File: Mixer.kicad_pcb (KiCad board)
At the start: 2 copper layers, 150 x 59 mm, 145 parts, among them J1 AudioJack3, J10 Conn_01x03, J11 Barrel_Jack_Switch, J2 AudioJack3, J3 USB_B_Micro, J4 Conn_01x03, J5 AudioJack3, J6 Conn_01x03, J7 AudioJack3, J8 Conn_01x03, J9 AudioJack3, SW1 SW_SPDT, SW2 SW_DPDT_x2, SW3 SW_DPDT_x2, U1 NJM4580CG, U10 NJM4580CG, U11 NJM4580CG, U12 SW_AKIDUKI, U2 NJM4580CG, U3 NJM4580CG, U4 MCW03, U5 MCW03, U6 NJM7809, U7 NJM7909, U8 NJM4580CG, U9 NJM4580CG

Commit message: 改版中
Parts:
- removed C48, C49: option_footprint, Capacitor_SMD:C_0603_1608Metric_Pad1.05x0.95mm_HandSolder
- removed G***: LOGO, toripoyo:tiemi
- removed J10, J6, J8: Conn_01x03, Connector_PinHeader_2.54mm:PinHeader_1x03_P2.54mm_Vertical
- removed RV2: RV10kA, toripoyo:RD925G-QA1
- added D14: 1N4148, Diode_SMD:D_SOD-123, F.Cu at (200.7, 110.5)
- added JP1: NoReg, Jumper:SolderJumper-2_P1.3mm_Open_TrianglePad1.0x1.5mm, F.Cu at (96.7, 128.3)
- added JP2: NoReg, Jumper:SolderJumper-2_P1.3mm_Open_TrianglePad1.0x1.5mm, F.Cu at (96.7, 131.8)
- added JP3: NoRect, Jumper:SolderJumper-2_P1.3mm_Open_TrianglePad1.0x1.5mm, F.Cu at (187.3, 146.0)
- added JP4: NoRect, Jumper:SolderJumper-2_P1.3mm_Open_TrianglePad1.0x1.5mm, F.Cu at (187.3, 151.0)
- added R23: 10k, Resistor_SMD:R_0603_1608Metric_Pad1.05x0.95mm_HandSolder, F.Cu at (162.3, 74.7)
- added R25: 10k, Resistor_SMD:R_0603_1608Metric_Pad1.05x0.95mm_HandSolder, F.Cu at (162.2, 77.6)
- added R26: 20k, Resistor_SMD:R_0603_1608Metric_Pad1.05x0.95mm_HandSolder, F.Cu at (197.6, 135.9)
- added R27: 10k, Resistor_SMD:R_0603_1608Metric_Pad1.05x0.95mm_HandSolder, F.Cu at (197.6, 138.4)
- added R28: 20k, Resistor_SMD:R_0603_1608Metric_Pad1.05x0.95mm_HandSolder, F.Cu at (202.0, 135.9)
- added R29: 10k, Resistor_SMD:R_0603_1608Metric_Pad1.05x0.95mm_HandSolder, F.Cu at (202.0, 138.4)
- added R30: 20k, Resistor_SMD:R_0603_1608Metric_Pad1.05x0.95mm_HandSolder, F.Cu at (206.3, 135.9)
- added R33: 20k, Resistor_SMD:R_0603_1608Metric_Pad1.05x0.95mm_HandSolder, F.Cu at (206.3, 138.4)
- added TP1: +9V, TestPoint:TestPoint_Pad_D1.5mm, F.Cu at (100.6, 128.3)
- added TP2: -9V, TestPoint:TestPoint_Pad_D1.5mm, F.Cu at (100.6, 131.8)
- added TP3: PH_L, TestPoint:TestPoint_Pad_D1.5mm, F.Cu at (193.0, 151.0)
- added TP4: PH_R, TestPoint:TestPoint_Pad_D1.5mm, F.Cu at (192.0, 147.0)
- C10, C11: value 4.7u -> 220u/6.3V; footprint Capacitor_THT:CP_Radial_D6.3mm_P2.50mm -> Capacitor_SMD:C_1210_3225Metric_Pad1.42x2.65mm_HandSolder; moved to B.Cu
- C12, C13, C18, C19: value 100u/16V -> 47u; footprint Capacitor_THT:CP_Radial_D5.0mm_P2.00mm -> Capacitor_SMD:C_1210_3225Metric_Pad1.42x2.65mm_HandSolder
- C14, C15: value 0.1u -> 47u; footprint Capacitor_SMD:C_0603_1608Metric_Pad1.05x0.95mm_HandSolder -> Capacitor_SMD:C_1210_3225Metric_Pad1.42x2.65mm_HandSolder; moved to F.Cu
- C16, C17: value 0.1u -> 47u; footprint Capacitor_SMD:C_0603_1608Metric_Pad1.05x0.95mm_HandSolder -> Capacitor_SMD:C_1210_3225Metric_Pad1.42x2.65mm_HandSolder
- C20: value 100u/6.3V -> 47u; footprint Capacitor_THT:CP_Radial_D5.0mm_P2.00mm -> Capacitor_SMD:C_1210_3225Metric_Pad1.42x2.65mm_HandSolder
- C21, C22, C23, C24: value 22u/16V -> 47u; footprint Capacitor_THT:CP_Radial_D5.0mm_P2.00mm -> Capacitor_SMD:C_1210_3225Metric_Pad1.42x2.65mm_HandSolder
- C35: value 0.47u -> 47u; footprint Capacitor_THT:CP_Radial_D5.0mm_P2.00mm -> Capacitor_SMD:C_1210_3225Metric_Pad1.42x2.65mm_HandSolder
- C36: value 22u/16V -> 220u/6.3V; footprint Capacitor_THT:CP_Radial_D5.0mm_P2.00mm -> Capacitor_SMD:C_1210_3225Metric_Pad1.42x2.65mm_HandSolder
- C39: value 22u/16V -> 22u/25V; footprint Capacitor_THT:CP_Radial_D5.0mm_P2.00mm -> Capacitor_SMD:C_0805_2012Metric_Pad1.15x1.40mm_HandSolder
- C40: value 0.47u -> 1u; footprint Capacitor_THT:C_Rect_L11.0mm_W4.2mm_P10.00mm_MKT -> Capacitor_SMD:C_0603_1608Metric_Pad1.05x0.95mm_HandSolder
- C41: value 0.47u -> 1u; footprint Capacitor_THT:C_Rect_L11.0mm_W4.2mm_P10.00mm_MKT -> Capacitor_SMD:C_0603_1608Metric_Pad1.05x0.95mm_HandSolder; moved to B.Cu
- C47: value 0.47u -> 22u/25V; footprint Capacitor_THT:CP_Radial_D5.0mm_P2.00mm -> Capacitor_SMD:C_0805_2012Metric_Pad1.15x1.40mm_HandSolder
- C50, C51: value option footprint -> 1u
- C53, C54, C55, C56: value 100u/16V -> 22u/25V; footprint Capacitor_THT:CP_Radial_D5.0mm_P2.00mm -> Capacitor_SMD:C_0805_2012Metric_Pad1.15x1.40mm_HandSolder
- D10, D12, D8, D9: value SS2040 -> 1N4148
- D11: value LED_RED -> LED_ORANGE
- D13: value LED_RED -> 1N4148; footprint LED_SMD:LED_0603_1608Metric_Pad1.05x0.95mm_HandSolder -> Diode_SMD:D_SOD-123
- J1, J2, J5, J7, J9: value AudioJack3 -> PJ-3420
- R13, R14: value 10k -> 33k
- R21, R24: value 470k -> 10k
- R31: value 4.7k -> 22k
- R32: value 4.7k -> 1.2k
- R35, R36: value 470 -> 1k
- R41, R42: value 100k -> 10k
- RV1, RV3, RV4, RV5: value RV10kA -> RK0972-A10K
- SW1: value SW_SPDT -> 2MS1-T1-B2-M7-S-E
- SW2, SW3: value SW_DPDT_x2 -> OS202011MA0QN1
- moved C35 98.9 mm to (100.3, 147.1), turned to 0 degrees
- moved C47 77.8 mm to (110.8, 146.4), turned to 0 degrees
- moved C41 35.9 mm to (171.2, 79.8), turned to 0 degrees
- moved C40 35.6 mm to (172.0, 76.2), turned to 90 degrees
- moved C16 14.0 mm to (103.5, 114.3)
- moved C17 14.0 mm to (86.4, 114.3)
- moved RV5 12.0 mm to (161.0, 114.0)
- moved C13 11.8 mm to (91.4, 89.3)
- moved C11 10.5 mm to (96.5, 81.9), turned to 180 degrees
- moved R35 6.84 mm to (196.8, 105.4)
- moved R36 6.38 mm to (200.7, 105.4)
- moved D13 6.25 mm to (196.8, 110.5)
- moved C14 6.21 mm to (106.0, 95.9)
- moved RV4 6.00 mm to (137.0, 114.0)
- moved C15 3.37 mm to (91.4, 95.9), turned to 90 degrees
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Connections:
- net BM64_MFB renamed BM62_MFB
- net BM64_SYS_PWR renamed BM62_SYS_PWR
- C20 pad 1: +5VD -> +9VA
- C20 pad 2: GND -> Net-(C20-Pad2)
- C21 pad 1: Net-(ANT1-Pad7) -> Net-(C20-Pad2)
- C21 pad 2: BT_in_R -> -9VA
- C22 pad 1: Net-(ANT1-Pad9) -> +9VA
- C22 pad 2: BT_in_L -> Net-(C20-Pad2)
- C23 pad 1: Net-(ANT1-Pad14) -> Net-(C20-Pad2)
- C23 pad 2: Net-(C23-Pad2) -> -9VA
- C24 pad 1: Net-(ANT1-Pad15) -> +9VA
- C24 pad 2: Net-(C24-Pad2) -> Net-(C20-Pad2)
- C35 pad 1: Net-(C35-Pad1) -> Net-(C20-Pad2)
- C35 pad 2: GND -> -9VA
- C36 pad 1: Net-(C36-Pad1) -> +5VD
- C37 pad 1: Net-(C36-Pad1) -> Net-(C37-Pad1)
- C39 pad 1: Net-(C38-Pad1) -> Net-(ANT1-Pad7)
- C39 pad 2: GND -> BT_in_R
- C45 pad 1: Net-(C45-Pad1) -> Net-(C40-Pad2)
- C46 pad 1: Net-(C46-Pad1) -> Net-(C41-Pad2)
- C47 pad 1: Net-(C47-Pad1) -> Net-(ANT1-Pad9)
- C47 pad 2: GND -> BT_in_L
- C50 pad 1: Net-(C40-Pad2) -> Net-(C50-Pad1)
- C50 pad 2: Net-(C40-Pad1) -> Net-(C50-Pad2)
- C51 pad 1: Net-(C41-Pad2) -> Net-(C51-Pad1)
- C51 pad 2: Net-(C41-Pad1) -> Net-(C51-Pad2)
- C53 pad 1: +9VA -> Net-(ANT1-Pad14)
- C53 pad 2: GND -> Net-(C53-Pad2)
- C54 pad 1: GND -> Net-(ANT1-Pad15)
- C54 pad 2: -9VA -> Net-(C54-Pad2)
- C55 pad 1: +9VA -> Net-(C37-Pad1)
- C56 pad 1: GND -> Net-(C38-Pad1)
- C56 pad 2: -9VA -> GND
- D10 pad 1: Net-(C47-Pad1) -> Net-(D10-Pad1)
- D12 pad 1: Net-(C35-Pad1) -> Net-(D12-Pad1)
- D13 pad 1: GND -> Net-(D11-Pad2)
- D2 pad 1: Net-(C24-Pad2) -> Net-(C54-Pad2)
- D5 pad 1: Net-(C23-Pad2) -> Net-(C53-Pad2)
- D8 pad 1: Net-(D10-Pad2) -> Net-(D8-Pad1)
- D8 pad 2: Net-(D8-Pad2) -> Net-(D10-Pad1)
- D9 pad 1: Net-(D12-Pad2) -> Net-(D9-Pad1)
- D9 pad 2: Net-(D9-Pad2) -> Net-(D12-Pad1)
- J9 pad R: Net-(C41-Pad1) -> Net-(C51-Pad2)
- J9 pad T: Net-(C40-Pad1) -> Net-(C50-Pad2)
- R15 pad 2: BT_Line_out_L -> mix_out_L
- R16 pad 2: BT_Line_out_R -> mix_out_R
- R19 pad 1: Net-(C23-Pad2) -> Net-(C53-Pad2)
- R19 pad 2: BT_Line_out_R -> mix_out_R
- R20 pad 1: Net-(C24-Pad2) -> Net-(C54-Pad2)
- R20 pad 2: BT_Line_out_L -> mix_out_L
- R21 pad 1: GND -> mix_out_L
- R21 pad 2: Net-(C47-Pad1) -> Net-(D8-Pad1)
- R24 pad 1: GND -> mix_out_R
- R24 pad 2: Net-(C35-Pad1) -> Net-(D9-Pad1)
- R36 pad 2: Net-(D11-Pad2) -> Net-(D14-Pad2)
- R37 pad 1: Net-(C36-Pad1) -> Net-(C37-Pad1)
- R38 pad 1: Net-(C36-Pad1) -> Net-(C37-Pad1)
- R38 pad 2: Net-(C40-Pad1) -> Net-(C50-Pad2)
- R39 pad 2: Net-(C41-Pad1) -> Net-(C51-Pad2)
- R41 pad 1: Net-(C40-Pad2) -> Net-(C50-Pad1)
- R42 pad 1: Net-(C41-Pad2) -> Net-(C51-Pad1)
- R46 pad 1: Net-(C45-Pad1) -> Net-(C40-Pad2)
- R47 pad 1: Net-(C46-Pad1) -> Net-(C41-Pad2)
- RV5 pad 3: Net-(C46-Pad1) -> Net-(C41-Pad1)
- RV5 pad 6: Net-(C45-Pad1) -> Net-(C40-Pad1)
- SW3 pad 1: Net-(C45-Pad1) -> Net-(C40-Pad2)
- SW3 pad 4: Net-(C46-Pad1) -> Net-(C41-Pad2)
- U10 pad 3: Net-(D8-Pad2) -> Net-(JP4-Pad2)
- U10 pad 5: Net-(D9-Pad2) -> Net-(JP3-Pad2)
- U11 pad 1: Net-(C45-Pad1) -> Net-(C40-Pad2)
- U11 pad 3: Net-(C40-Pad2) -> Net-(C50-Pad1)
- U11 pad 5: Net-(C41-Pad2) -> Net-(C51-Pad1)
- U11 pad 7: Net-(C46-Pad1) -> Net-(C41-Pad2)
- U8 pad 1: Net-(D12-Pad2) -> Net-(D12-Pad1)
- U8 pad 2: Net-(D9-Pad2) -> Net-(D9-Pad1)
- U8 pad 3: mix_out_R -> GND
- U8 pad 5: Net-(C35-Pad1) -> GND
- U8 pad 6: Net-(D9-Pad2) -> Net-(R28-Pad2)
- U8 pad 7: Net-(D9-Pad2) -> Net-(JP3-Pad2)
- U9 pad 1: Net-(D10-Pad2) -> Net-(D10-Pad1)
- U9 pad 2: Net-(D8-Pad2) -> Net-(D8-Pad1)
- U9 pad 3: mix_out_L -> GND
- U9 pad 5: Net-(C47-Pad1) -> GND
- U9 pad 6: Net-(D8-Pad2) -> Net-(R26-Pad2)
- U9 pad 7: Net-(D8-Pad2) -> Net-(JP4-Pad2)
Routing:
- net +9VA: track 258.6 -> 0.00 mm, vias 12 -> 0
- net -9VA: track 236.3 -> 0.00 mm, vias 9 -> 0
- net Net-(C46-Pad1): track 123.4 -> 0.00 mm, vias 2 -> 0
- net Net-(C45-Pad1): track 111.5 -> 0.00 mm, vias 2 -> 0
- net +5VD: track 108.0 -> 0.00 mm, vias 1 -> 0
- net BT_Line_out_L: track 94.2 -> 0.00 mm, vias 3 -> 0
- net BT_Line_out_R: track 91.3 -> 0.00 mm, vias 3 -> 0
- net mix_out_L: track 90.0 -> 0.00 mm
- net Net-(RV4-Pad3): track 88.9 -> 0.00 mm
- net Net-(RV4-Pad6): track 82.3 -> 0.00 mm
- net mix_out_R: track 84.8 -> 6.74 mm, vias 3 -> 0
- net BT_in_L: track 76.3 -> 0.00 mm
- net BT_in_R: track 74.9 -> 0.00 mm
- net Net-(J5-PadR): track 74.0 -> 0.00 mm, vias 1 -> 0
- net Net-(J5-PadT): track 70.1 -> 0.00 mm
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- added copper zone on B.Cu, net +9VA
- added copper zone on -V, net -9VA
- added copper zone on GND, net GND
- removed copper zone on B.Cu, net GND
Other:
- copper layers 2 -> 4
- board text removed: "Opt."
- board text removed: "To BT /Line Out"

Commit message: Rev.A 作成中
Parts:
- removed C23, C24, C35: 47u, Capacitor_SMD:C_1210_3225Metric_Pad1.42x2.65mm_HandSolder
- removed C3, C32, C37, C38, C52, C6, C9: 0.1u, Capacitor_SMD:C_0603_1608Metric_Pad1.05x0.95mm_HandSolder
- removed C36: 220u/6.3V, Capacitor_SMD:C_1210_3225Metric_Pad1.42x2.65mm_HandSolder
- removed C51: 1u, Capacitor_SMD:C_0603_1608Metric_Pad1.05x0.95mm_HandSolder
- removed C53, C54, C55, C56: 22u/25V, Capacitor_SMD:C_0805_2012Metric_Pad1.15x1.40mm_HandSolder
- removed D10, D13, D14, D8, D9: 1N4148, Diode_SMD:D_SOD-123
- removed D11: LED_ORANGE, LED_SMD:LED_0603_1608Metric_Pad1.05x0.95mm_HandSolder
- removed J11: Barrel_Jack_Switch, hastech:MJ-179P
- removed JP3, JP4: NoRect, Jumper:SolderJumper-2_P1.3mm_Open_TrianglePad1.0x1.5mm
- removed R43, R44: 1k, Resistor_SMD:R_0603_1608Metric_Pad1.05x0.95mm_HandSolder
- removed R45, R48: 10k, Resistor_SMD:R_0603_1608Metric_Pad1.05x0.95mm_HandSolder
- removed R46, R47: 100k, Resistor_SMD:R_0603_1608Metric_Pad1.05x0.95mm_HandSolder
- removed RV5: RK0972-A10K, toripoyo:RD925G-QA1
- removed TP1: +9V, TestPoint:TestPoint_Pad_D1.5mm
- removed TP2: -9V, TestPoint:TestPoint_Pad_D1.5mm
- removed TP3: PH_L, TestPoint:TestPoint_Pad_D1.5mm
- removed TP4: PH_R, TestPoint:TestPoint_Pad_D1.5mm
- removed U10: NJM4580CG, Package_SO:SOP-8_3.9x4.9mm_P1.27mm
- removed U12: SW_AKIDUKI, hastech:SW_AKZK
- added C48: 0.1u, Capacitor_SMD:C_0603_1608Metric_Pad1.05x0.95mm_HandSolder, F.Cu at (185.2, 80.5)
- added C49: 1u, Capacitor_SMD:C_0603_1608Metric_Pad1.05x0.95mm_HandSolder, F.Cu at (173.5, 79.0)
- added J10: Conn_01x03, Connector_PinSocket_2.54mm:PinSocket_1x03_P2.54mm_Vertical, F.Cu at (185.9, 92.5)
- added J6: PJ-3420, toripoyo:PJ-3420, F.Cu at (162.4, 57.4)
- added J8: PJ-3420, toripoyo:PJ-3420, F.Cu at (201.0, 57.3)
- added R34: 1k, Resistor_SMD:R_0603_1608Metric_Pad1.05x0.95mm_HandSolder, F.Cu at (191.3, 81.0)
- added RV2: RK0972-A10K, toripoyo:RD925G-QA1, F.Cu at (113.0, 114.0)
- C10: value 220u/6.3V -> 0.1u; footprint Capacitor_SMD:C_1210_3225Metric_Pad1.42x2.65mm_HandSolder -> Capacitor_SMD:C_0603_1608Metric_Pad1.05x0.95mm_HandSolder; moved to F.Cu
- C12: value 47u -> 220u/6.3V; moved to B.Cu
- C13, C14, C15, C16, C17, C18, C19, C20, JP1, JP2: moved to B.Cu
- C25: value 0.1u -> 47u; footprint Capacitor_SMD:C_0603_1608Metric_Pad1.05x0.95mm_HandSolder -> Capacitor_SMD:C_1210_3225Metric_Pad1.42x2.65mm_HandSolder; moved to F.Cu
- C26: value 0.1u -> 47u; footprint Capacitor_SMD:C_0603_1608Metric_Pad1.05x0.95mm_HandSolder -> Capacitor_SMD:C_1210_3225Metric_Pad1.42x2.65mm_HandSolder
- C27: value 0.1u -> 220u/6.3V; footprint Capacitor_SMD:C_0603_1608Metric_Pad1.05x0.95mm_HandSolder -> Capacitor_SMD:C_1210_3225Metric_Pad1.42x2.65mm_HandSolder; moved to B.Cu
- C28, C29, C30, C31, C42: value 0.1u -> 22u/25V; footprint Capacitor_SMD:C_0603_1608Metric_Pad1.05x0.95mm_HandSolder -> Capacitor_SMD:C_0805_2012Metric_Pad1.15x1.40mm_HandSolder
- C40: value 1u -> 0.1u
- C41: value 1u -> 0.1u; moved to F.Cu
- C43, C44: value 0.1u -> 1u
- C47: value 22u/25V -> 0.1u; footprint Capacitor_SMD:C_0805_2012Metric_Pad1.15x1.40mm_HandSolder -> Capacitor_SMD:C_0603_1608Metric_Pad1.05x0.95mm_HandSolder
- D12: value 1N4148 -> LED_ORANGE; footprint Diode_SMD:D_SOD-123 -> LED_SMD:LED_0603_1608Metric_Pad1.05x0.95mm_HandSolder
- J3: value USB_B_Micro -> Barrel_Jack_Switch; footprint toripoyo:USB_Micro_B_Female_10118193-0001LF -> hastech:MJ-179P
- J4: value Conn_01x03 -> USB_B_Micro; footprint Connector_PinHeader_2.54mm:PinHeader_1x03_P2.54mm_Vertical -> toripoyo:USB_Micro_B_Female_10118193-0001LF
- J5: value PJ-3420 -> Conn_01x03; footprint toripoyo:PJ-3420 -> Connector_PinHeader_2.54mm:PinHeader_1x03_P2.54mm_Vertical
- J9: value PJ-3420 -> Conn_01x03; footprint toripoyo:PJ-3420 -> Connector_PinSocket_2.54mm:PinSocket_1x03_P2.54mm_Vertical
- R1, R5: value 10 -> 47k
- R10, R9: value 47k -> 10k
- R11, R12, R24: value 10k -> 33k
- R13, R14: value 33k -> 600
- R15, R16: value 600 -> 10
- R18: moved to F.Cu
- R21: value 10k -> 2k; moved to B.Cu
- R22: value 2k -> 22k; moved to F.Cu
- R23, R42: value 10k -> 1.2k
- R25: value 10k -> 8.2k
- R26: value 20k -> 4.7k
- R27: value 10k -> 4.7
- R28: value 20k -> 2k?
- R29: value 10k -> 2k?
- R30: value 20k -> 4.7
- R31: value 22k -> 10k
- R32: value 1.2k -> 10k
- R33: value 20k -> 1k
- R35: value 1k -> 100k
- R36: value 1k -> 10k
- R37: value 4.7 -> 100k
- R38: value 2k? -> 10k
- R39: value 2k? -> 33k
- R40: value 4.7 -> 8.2k
- R41: value 10k -> 22k
- U8: value NJM4580CG -> SW_AKIDUKI; footprint Package_SO:SOP-8_3.9x4.9mm_P1.27mm -> hastech:SW_AKZK
- U9: value NJM4580CG -> LM339PWR; footprint Package_SO:SOP-8_3.9x4.9mm_P1.27mm -> Package_SO:TSSOP-14_4.4x5mm_P0.65mm
- moved C47 104.9 mm to (185.2, 72.4), turned to 180 degrees
- moved C26 101.8 mm to (85.7, 128.9), turned to 0 degrees
- moved R22 89.7 mm to (194.6, 96.8), turned to 90 degrees
- moved C28 78.8 mm to (114.0, 78.0), turned to 90 degrees
- moved U8 78.8 mm to (114.2, 63.0), turned to 180 degrees
- moved R16 78.0 mm to (213.1, 103.1), turned to 90 degrees
- moved R15 67.8 mm to (205.2, 102.9), turned to 90 degrees
- moved C21 65.9 mm to (79.5, 134.6)
- moved C27 65.9 mm to (126.0, 82.5), turned to 90 degrees
- moved R21 64.9 mm to (110.5, 65.3), turned to 0 degrees
- moved R33 64.4 mm to (179.1, 80.0), turned to 180 degrees
- moved C25 64.0 mm to (79.4, 128.9)
- moved R1 61.8 mm to (143.5, 97.3), turned to 270 degrees
- moved R29 59.9 mm to (209.3, 79.0)
- moved R28 59.2 mm to (218.2, 79.0)
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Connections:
- C10 pad 1: +5VD -> Net-(C10-Pad1)
- C12 pad 1: Net-(C12-Pad1) -> +5VD
- C13 pad 1: GND -> Net-(C13-Pad1)
- C13 pad 2: Net-(C13-Pad2) -> GND
- C14 pad 1: Net-(C12-Pad1) -> GND
- C14 pad 2: GND -> Net-(C14-Pad2)
- C15 pad 1: GND -> Net-(C13-Pad1)
- C15 pad 2: Net-(C13-Pad2) -> GND
- C16 pad 1: +9VA -> GND
- C16 pad 2: GND -> Net-(C14-Pad2)
- C17 pad 1: GND -> +9VA
- C17 pad 2: -9VA -> GND
- C18 pad 1: +9VA -> GND
- C18 pad 2: GND -> -9VA
- C19 pad 1: GND -> +9VA
- C19 pad 2: -9VA -> GND
- C20 pad 1: +9VA -> GND
- C20 pad 2: Net-(C20-Pad2) -> -9VA
- C21 pad 1: Net-(C20-Pad2) -> +9VA
- C21 pad 2: -9VA -> GND
- C22 pad 1: +9VA -> GND
- C22 pad 2: Net-(C20-Pad2) -> -9VA
- C25 pad 1: +5VD -> +9VA
- C26 pad 1: +9VA -> GND
- C26 pad 2: GND -> -9VA
- C27 pad 1: GND -> +5VD
- C27 pad 2: -9VA -> GND
- C28 pad 1: +9VA -> Net-(ANT1-Pad7)
- C28 pad 2: -9VA -> BT_in_R
- C29 pad 1: +9VA -> Net-(ANT1-Pad9)
- C29 pad 2: GND -> BT_in_L
- C30 pad 1: GND -> Net-(ANT1-Pad14)
- C30 pad 2: -9VA -> Net-(C30-Pad2)
- C31 pad 1: +9VA -> Net-(ANT1-Pad15)
- C31 pad 2: -9VA -> Net-(C31-Pad2)
- C33 pad 1: GND -> +9VA
- C33 pad 2: -9VA -> GND
- C34 pad 1: +9VA -> -9VA
- C34 pad 2: -9VA -> GND
- C39 pad 1: Net-(ANT1-Pad7) -> Net-(C39-Pad1)
- C39 pad 2: BT_in_R -> GND
- C40 pad 1: Net-(C40-Pad1) -> Net-(C39-Pad1)
- C40 pad 2: Net-(C40-Pad2) -> GND
- C41 pad 2: Net-(C41-Pad2) -> GND
- C42 pad 1: +9VA -> Net-(C41-Pad1)
- C43 pad 1: GND -> Net-(C43-Pad1)
- C43 pad 2: -9VA -> Net-(C43-Pad2)
- C44 pad 1: +9VA -> Net-(C44-Pad1)
- C44 pad 2: -9VA -> Net-(C44-Pad2)
- C45 pad 1: Net-(C40-Pad2) -> Net-(C45-Pad1)
- C46 pad 1: Net-(C41-Pad2) -> Net-(C46-Pad1)
- C47 pad 1: Net-(ANT1-Pad9) -> +9VA
- C47 pad 2: BT_in_L -> GND
- C50 pad 2: Net-(C50-Pad2) -> Net-(C46-Pad1)
- D2 pad 1: Net-(C54-Pad2) -> GND
- D3 pad 1: GND -> Net-(C30-Pad2)
- D4 pad 1: GND -> Net-(C31-Pad2)
- D5 pad 1: Net-(C53-Pad2) -> GND
- J3 pad 1: Net-(J11-Pad1) -> Net-(J3-Pad1)
- J3 pad 2: Net-(J3-Pad2) -> GND
- J3 pad 3: Net-(J3-Pad3) -> (no net)
- J4 pad 1: Net-(ANT1-Pad32) -> Net-(J3-Pad1)
- J4 pad 2: Net-(ANT1-Pad33) -> Net-(J4-Pad2)
- J4 pad 3: GND -> Net-(J4-Pad3)
- JP1 pad 1: Net-(C12-Pad1) -> Net-(C13-Pad1)
- JP2 pad 1: Net-(C13-Pad2) -> Net-(C14-Pad2)
- R1 pad 1: Net-(J2-PadT) -> Net-(R1-Pad1)
- R1 pad 2: Net-(R1-Pad2) -> in3_L
- R11 pad 1: Net-(R11-Pad1) -> mix_out_L
- R12 pad 1: Net-(R12-Pad1) -> mix_out_R
- R13 pad 1: mix_out_L -> Net-(J1-PadT)
- R13 pad 2: Net-(R11-Pad1) -> mix_out_L
- R14 pad 1: mix_out_R -> Net-(J1-PadR)
- R14 pad 2: Net-(R12-Pad1) -> mix_out_R
- R15 pad 1: Net-(J1-PadT) -> Net-(J2-PadT)
- R15 pad 2: mix_out_L -> Net-(R15-Pad2)
- R16 pad 1: Net-(J1-PadR) -> Net-(J2-PadR)
- R16 pad 2: mix_out_R -> Net-(R16-Pad2)
- R18 pad 1: Net-(J3-Pad2) -> Net-(J4-Pad2)
- R18 pad 2: Net-(J3-Pad3) -> Net-(J4-Pad3)
- R19 pad 1: Net-(C53-Pad2) -> Net-(C30-Pad2)
- R2 pad 1: Net-(R2-Pad1) -> Net-(R1-Pad1)
- R2 pad 2: in3_L -> in2_L
- R20 pad 1: Net-(C54-Pad2) -> Net-(C31-Pad2)
- R21 pad 1: mix_out_L -> GND
- R21 pad 2: Net-(D8-Pad1) -> BM62_MFB
- R22 pad 1: GND -> Net-(J9-Pad3)
- R22 pad 2: BM62_MFB -> +9VA
- R23 pad 1: Net-(D8-Pad1) -> GND
- R23 pad 2: Net-(D10-Pad2) -> Net-(J9-Pad3)
- R24 pad 1: mix_out_R -> Net-(J9-Pad1)
- R24 pad 2: Net-(D9-Pad1) -> +9VA
- R25 pad 1: Net-(D9-Pad1) -> GND
- R25 pad 2: Net-(D12-Pad2) -> Net-(J9-Pad1)
- R26 pad 1: mix_out_L -> +9VA
- R26 pad 2: Net-(R26-Pad2) -> Net-(D12-Pad2)
- R27 pad 1: Net-(D10-Pad2) -> Net-(C39-Pad1)
- R27 pad 2: Net-(R26-Pad2) -> +9VA
- R28 pad 1: mix_out_R -> Net-(C39-Pad1)
- R28 pad 2: Net-(R28-Pad2) -> Net-(C43-Pad2)
- R29 pad 1: Net-(D12-Pad2) -> Net-(C41-Pad1)
- R29 pad 2: Net-(R28-Pad2) -> Net-(C44-Pad2)
- R3 pad 1: Net-(R2-Pad1) -> Net-(R1-Pad1)
- R3 pad 2: in2_L -> in1_L
- R30 pad 1: Net-(R26-Pad2) -> Net-(C41-Pad1)
- R30 pad 2: Net-(JP4-Pad2) -> +9VA
- R31 pad 1: Net-(R31-Pad1) -> Net-(C43-Pad1)
- R31 pad 2: +9VA -> GND
- R32 pad 1: GND -> Net-(C44-Pad1)
- R32 pad 2: Net-(R31-Pad1) -> GND
- R33 pad 1: Net-(R28-Pad2) -> Net-(C45-Pad2)
- R33 pad 2: Net-(JP3-Pad2) -> GND
- R35 pad 1: Net-(R35-Pad1) -> Net-(C45-Pad1)
- R35 pad 2: Net-(D13-Pad2) -> Net-(C45-Pad2)
- R36 pad 2: Net-(D14-Pad2) -> Net-(C45-Pad2)
- R37 pad 1: Net-(C37-Pad1) -> Net-(C46-Pad1)
- R37 pad 2: +9VA -> Net-(C46-Pad2)
- R38 pad 1: Net-(C37-Pad1) -> Net-(R38-Pad1)
- R38 pad 2: Net-(C50-Pad2) -> Net-(C46-Pad2)
- R39 pad 1: Net-(C38-Pad1) -> Net-(J10-Pad1)
- R39 pad 2: Net-(C51-Pad2) -> GND
- R4 pad 1: Net-(R2-Pad1) -> Net-(R4-Pad1)
- R4 pad 2: in1_L -> in3_R
- R40 pad 1: Net-(C38-Pad1) -> -9VA
- R40 pad 2: +9VA -> Net-(J10-Pad1)
- R41 pad 1: Net-(C50-Pad1) -> Net-(J10-Pad3)
- R42 pad 1: Net-(C51-Pad1) -> -9VA
- R42 pad 2: GND -> Net-(J10-Pad3)
- R5 pad 1: Net-(J2-PadR) -> Net-(R4-Pad1)
- R5 pad 2: Net-(R5-Pad2) -> in2_R
- R6 pad 1: Net-(R10-Pad2) -> Net-(R4-Pad1)
- R6 pad 2: in3_R -> in1_R
- R7 pad 1: Net-(R10-Pad2) -> Net-(R7-Pad1)
- R7 pad 2: in2_R -> Net-(R1-Pad1)
- R8 pad 2: in1_R -> Net-(R4-Pad1)
- R9 pad 2: Net-(R2-Pad1) -> Net-(R7-Pad1)
- RV1 pad 3: mix_out_R -> mix_out_L
- RV1 pad 6: mix_out_L -> mix_out_R
- RV3 pad 2: in1_R -> in2_R
- RV3 pad 3: Net-(J5-PadR) -> Net-(RV3-Pad3)
- RV3 pad 5: in1_L -> in2_L
- RV3 pad 6: Net-(J5-PadT) -> Net-(RV3-Pad6)
- RV4 pad 2: in2_R -> in3_R
- RV4 pad 3: Net-(RV4-Pad3) -> Net-(C50-Pad1)
- RV4 pad 5: in2_L -> in3_L
- RV4 pad 6: Net-(RV4-Pad6) -> Net-(C49-Pad1)
- SW1 pad 1: Net-(J11-Pad1) -> Net-(J3-Pad1)
- SW2 pad 1: Net-(J7-PadT) -> Net-(J6-PadT)
- SW2 pad 2: Net-(RV4-Pad6) -> Net-(RV3-Pad6)
- SW2 pad 4: Net-(J7-PadR) -> Net-(J6-PadR)
- SW2 pad 5: Net-(RV4-Pad3) -> Net-(RV3-Pad3)
- SW3 pad 1: Net-(C40-Pad2) -> Net-(C45-Pad1)
- SW3 pad 2: Net-(R45-Pad1) -> Net-(R36-Pad1)
- SW3 pad 4: Net-(C41-Pad2) -> Net-(C46-Pad1)
- SW3 pad 5: Net-(R48-Pad1) -> Net-(R38-Pad1)
- U1 pad 1: Net-(R11-Pad2) -> Net-(R7-Pad1)
- U1 pad 2: Net-(R2-Pad1) -> Net-(R1-Pad1)
- U1 pad 6: Net-(R11-Pad1) -> Net-(R11-Pad2)
- U11 pad 1: Net-(C40-Pad2) -> Net-(C45-Pad1)
- U11 pad 3: Net-(C50-Pad1) -> Net-(C43-Pad1)
- U11 pad 5: Net-(C51-Pad1) -> Net-(C44-Pad1)
- U11 pad 7: Net-(C41-Pad2) -> Net-(C46-Pad1)
- U2 pad 1: Net-(R10-Pad1) -> Net-(R10-Pad2)
- U2 pad 2: Net-(R10-Pad2) -> Net-(R4-Pad1)
- U2 pad 6: Net-(R12-Pad1) -> Net-(R10-Pad1)
- U3 pad 1: Net-(R1-Pad2) -> Net-(R15-Pad2)
- U3 pad 2: Net-(R1-Pad2) -> Net-(R15-Pad2)
- U3 pad 3: Net-(RV1-Pad5) -> Net-(RV1-Pad2)
- U3 pad 5: Net-(RV1-Pad2) -> Net-(RV1-Pad5)
- U3 pad 6: Net-(R5-Pad2) -> Net-(R16-Pad2)
- U3 pad 7: Net-(R5-Pad2) -> Net-(R16-Pad2)
- U4 pad 6: Net-(C12-Pad1) -> Net-(C13-Pad1)
- U5 pad 7: Net-(C13-Pad2) -> Net-(C14-Pad2)
- U6 pad 1: Net-(C12-Pad1) -> Net-(C13-Pad1)
- U7 pad 2: Net-(C13-Pad2) -> Net-(C14-Pad2)
- U9 pad 1: Net-(D10-Pad1) -> Net-(D12-Pad1)
- U9 pad 2: Net-(D8-Pad1) -> Net-(D12-Pad1)
- U9 pad 3: GND -> +9VA
- U9 pad 4: -9VA -> vref_out_-
- U9 pad 5: GND -> mix_out_L
- U9 pad 6: Net-(R26-Pad2) -> mix_out_L
- U9 pad 7: Net-(JP4-Pad2) -> vref_out_+
- U9 pad 8: +9VA -> mix_out_R
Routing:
- net +5VD: track 0.00 -> 83.0 mm, vias 0 -> 1
- net Net-(J3-Pad1): track 0.00 -> 55.1 mm
- net Net-(J6-PadR): track 0.00 -> 25.7 mm
- net Net-(C13-Pad1): track 0.00 -> 23.5 mm
- net Net-(C14-Pad2): track 0.00 -> 21.0 mm
- net +9VA: track 0.00 -> 16.4 mm
- net -9VA: track 0.00 -> 15.4 mm
- net Net-(C10-Pad1): track 0.00 -> 14.2 mm
- net BM62_SYS_PWR: track 0.00 -> 13.6 mm
- net BM62_MFB: track 0.00 -> 8.86 mm
- net Net-(C39-Pad1): track 0.00 -> 8.75 mm
- net Net-(C41-Pad1): track 0.00 -> 8.75 mm
- net Net-(C45-Pad1): track 0.00 -> 6.96 mm
- net Net-(C46-Pad1): track 0.00 -> 6.85 mm
- net mix_out_R: track 6.74 -> 0.00 mm
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- added copper zone on B.Cu, net GND
- removed copper zone on B.Cu, net +9VA
- removed copper zone on -V, net -9VA
- removed copper zone on GND, net GND
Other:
- copper layers 4 -> 2
- board text added: "2020/8/24 poyo"
- board text removed: "2020/7/24 poyo"

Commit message: Rev.A 完成
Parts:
- removed C19, C20: 47u, Capacitor_SMD:C_1210_3225Metric_Pad1.42x2.65mm_HandSolder
- removed D5: VESD01-02V-G-08, Diode_SMD:D_SOD-523
- removed J10, J9: Conn_01x03, Connector_PinSocket_2.54mm:PinSocket_1x03_P2.54mm_Vertical
- removed U8: SW_AKIDUKI, hastech:SW_AKZK
- added C23: 0.1u, Capacitor_SMD:C_0603_1608Metric_Pad1.05x0.95mm_HandSolder, F.Cu at (153.0, 78.9)
- added C24: 0.1u, Capacitor_SMD:C_0603_1608Metric_Pad1.05x0.95mm_HandSolder, F.Cu at (150.5, 91.3)
- added C3: 0.1u, Capacitor_SMD:C_0603_1608Metric_Pad1.05x0.95mm_HandSolder, F.Cu at (165.7, 91.3)
- added C6: 0.1u, Capacitor_SMD:C_0603_1608Metric_Pad1.05x0.95mm_HandSolder, F.Cu at (153.0, 91.3)
- added C9: 0.1u, Capacitor_SMD:C_0603_1608Metric_Pad1.05x0.95mm_HandSolder, F.Cu at (165.7, 78.9)
- added R43: 4.7k, Resistor_SMD:R_0603_1608Metric_Pad1.05x0.95mm_HandSolder, F.Cu at (148.5, 101.9)
- added R44: 4.7k, Resistor_SMD:R_0603_1608Metric_Pad1.05x0.95mm_HandSolder, F.Cu at (146.4, 97.9)
- added R45: 4.7k, Resistor_SMD:R_0603_1608Metric_Pad1.05x0.95mm_HandSolder, F.Cu at (146.4, 101.9)
- added R46: 100, Resistor_SMD:R_0603_1608Metric_Pad1.05x0.95mm_HandSolder, F.Cu at (160.1, 78.9)
- added R47: 100, Resistor_SMD:R_0603_1608Metric_Pad1.05x0.95mm_HandSolder, F.Cu at (147.4, 78.9)
- added R48: 10k, Resistor_SMD:R_0603_1608Metric_Pad1.05x0.95mm_HandSolder, B.Cu at (210.7, 88.8)
- added R49: 10k, Resistor_SMD:R_0603_1608Metric_Pad1.05x0.95mm_HandSolder, B.Cu at (210.7, 91.7)
- added R50: 1k, Resistor_SMD:R_0603_1608Metric_Pad1.05x0.95mm_HandSolder, B.Cu at (215.2, 88.8)
- added R51: 1k, Resistor_SMD:R_0603_1608Metric_Pad1.05x0.95mm_HandSolder, B.Cu at (215.2, 91.7)
- added R52: 100, Resistor_SMD:R_0603_1608Metric_Pad1.05x0.95mm_HandSolder, F.Cu at (212.6, 88.8)
- added R53: 100, Resistor_SMD:R_0603_1608Metric_Pad1.05x0.95mm_HandSolder, F.Cu at (212.6, 90.8)
- added R54: 100, Resistor_SMD:R_0603_1608Metric_Pad1.05x0.95mm_HandSolder, F.Cu at (131.3, 99.8)
- added SW4: OS202011MA0QN1, digikey-download:OS202011MA0QN1, F.Cu at (215.4, 87.4)
- added SW5: OS202011MA0QN1, digikey-download:OS202011MA0QN1, F.Cu at (215.4, 74.6)
- added SW6: SW_Push, Button_Switch_THT:SW_PUSH_6mm, F.Cu at (115.8, 62.2)
- added U10: LM339PWR, Package_SO:TSSOP-14_4.4x5mm_P0.65mm, F.Cu at (151.0, 85.2)
- C13, C14, C15, C17, C18, C27: moved to F.Cu
- C25: value 47u -> 0.1u; footprint Capacitor_SMD:C_1210_3225Metric_Pad1.42x2.65mm_HandSolder -> Capacitor_SMD:C_0603_1608Metric_Pad1.05x0.95mm_HandSolder
- C26: value 47u -> 1u; footprint Capacitor_SMD:C_1210_3225Metric_Pad1.42x2.65mm_HandSolder -> Capacitor_SMD:C_0603_1608Metric_Pad1.05x0.95mm_HandSolder
- C30: value 22u/25V -> 1u; footprint Capacitor_SMD:C_0805_2012Metric_Pad1.15x1.40mm_HandSolder -> Capacitor_SMD:C_0603_1608Metric_Pad1.05x0.95mm_HandSolder
- C31: value 22u/25V -> 0.1u; footprint Capacitor_SMD:C_0805_2012Metric_Pad1.15x1.40mm_HandSolder -> Capacitor_SMD:C_0603_1608Metric_Pad1.05x0.95mm_HandSolder
- D12: value LED_ORANGE -> LED_RED
- D2, D4: value VESD01-02V-G-08 -> LED_GREEN; footprint Diode_SMD:D_SOD-523 -> LED_SMD:LED_0603_1608Metric_Pad1.05x0.95mm_HandSolder
- D3: value VESD01-02V-G-08 -> LED_RED; footprint Diode_SMD:D_SOD-523 -> LED_SMD:LED_0603_1608Metric_Pad1.05x0.95mm_HandSolder
- H1, H2, H3, H4: value MountingHole_Pad -> MountingHole; footprint MountingHole:MountingHole_3.2mm_M3_DIN965_Pad -> MountingHole:MountingHole_3.2mm_M3
- J3: value Barrel_Jack_Switch -> Conn_02x02_Counter_Clockwise; footprint hastech:MJ-179P -> Connector_PinHeader_2.54mm:PinHeader_2x02_P2.54mm_Vertical
- JP1: value NoReg -> UserShort; footprint Jumper:SolderJumper-2_P1.3mm_Open_TrianglePad1.0x1.5mm -> Jumper:SolderJumper-2_P1.3mm_Open_RoundedPad1.0x1.5mm
- JP2: value NoReg -> UserShort; footprint Jumper:SolderJumper-2_P1.3mm_Open_TrianglePad1.0x1.5mm -> Jumper:SolderJumper-2_P1.3mm_Open_RoundedPad1.0x1.5mm; moved to F.Cu
- R17: value 1k -> 4.7k
- R19: value 2k -> 33k
- R20: value 2k -> 1.2k
- R24: value 33k -> 1.2k
- R25: value 8.2k -> 33k
- R27, R30: value 4.7 -> 470
- R39: value 33k -> 100
- R40: value 8.2k -> 100
- moved H2 149.6 mm to (221.0, 64.0)
- moved H4 135.6 mm to (94.0, 115.0)
- moved C21 131.0 mm to (206.5, 102.5), turned to 270 degrees
- moved C22 121.7 mm to (202.4, 102.5), turned to 90 degrees
- moved C30 93.0 mm to (209.8, 89.7), turned to 90 degrees
- moved C25 87.0 mm to (150.5, 78.9), turned to 90 degrees
- moved C14 85.2 mm to (166.9, 101.0), turned to 180 degrees
- moved JP2 62.6 mm to (143.6, 83.3), turned to 0 degrees
- moved C13 61.6 mm to (166.9, 96.4)
- moved J3 50.8 mm to (127.8, 101.1), turned to 180 degrees
- moved R40 50.8 mm to (147.4, 91.3)
- moved C26 46.6 mm to (122.2, 99.8), turned to 90 degrees
- moved R24 45.9 mm to (155.8, 78.9)
- moved R25 45.9 mm to (155.8, 82.9)
- moved D2 40.2 mm to (156.8, 102.0)
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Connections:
- net Net-(J9-Pad1) renamed vref_out_-_-13dBv
- ANT1 pad 11: (no net) -> BT_Mic_Out_P
- ANT1 pad 12: (no net) -> BT_Mic_Out_N
- ANT1 pad 14: Net-(ANT1-Pad14) -> (no net)
- ANT1 pad 15: Net-(ANT1-Pad15) -> (no net)
- ANT1 pad 23: GND -> GNDD
- ANT1 pad 3: (no net) -> GNDD
- ANT1 pad 37: GND -> GNDD
- C10 pad 2: GND -> GNDD
- C11 pad 2: GND -> GNDD
- C12 pad 2: GND -> GNDD
- C13 pad 1: Net-(C13-Pad1) -> +9VA
- C13 pad 2: GND -> GND2
- C14 pad 1: GND -> GND2
- C14 pad 2: Net-(C14-Pad2) -> -9VA
- C15 pad 1: Net-(C13-Pad1) -> Net-(C15-Pad1)
- C16 pad 2: Net-(C14-Pad2) -> Net-(C16-Pad2)
- C25 pad 1: +9VA -> Net-(C25-Pad1)
- C25 pad 2: GND -> GND2
- C26 pad 2: -9VA -> BT_Mic_Out_N
- C27 pad 2: GND -> GNDD
- C30 pad 1: Net-(ANT1-Pad14) -> BT_Mic_Out_P
- C31 pad 1: Net-(ANT1-Pad15) -> GNDD
- C31 pad 2: Net-(C31-Pad2) -> GND
- C33 pad 1: +9VA -> Net-(C33-Pad1)
- C33 pad 2: GND -> GND2
- C34 pad 1: -9VA -> Net-(C34-Pad1)
- C34 pad 2: GND -> GND2
- D1 pad 1: GND -> -9VA
- D2 pad 1: GND -> Net-(D2-Pad1)
- D3 pad 1: Net-(C30-Pad2) -> Net-(D3-Pad1)
- D3 pad 2: Net-(D2-Pad2) -> Net-(D3-Pad2)
- D4 pad 1: Net-(C31-Pad2) -> Net-(D4-Pad1)
- H1 pad 1: GND -> (no net)
- H2 pad 1: GND -> (no net)
- H3 pad 1: GND -> (no net)
- H4 pad 1: GND -> (no net)
- J3 pad 1: Net-(J3-Pad1) -> GND
- J3 pad 3: (no net) -> GNDD
- J4 pad 1: Net-(J3-Pad1) -> Net-(J4-Pad1)
- J4 pad 5: GND -> GNDD
- J5 pad 3: GND -> GNDD
- JP1 pad 1: Net-(C13-Pad1) -> GND
- JP1 pad 2: +9VA -> GNDD
- JP2 pad 1: Net-(C14-Pad2) -> GND
- JP2 pad 2: -9VA -> GND2
- R17 pad 2: +5VD -> GND
- R19 pad 1: Net-(C30-Pad2) -> vref_out_+_-13dBv
- R19 pad 2: mix_out_R -> +9VA
- R20 pad 1: Net-(C31-Pad2) -> GND2
- R20 pad 2: mix_out_L -> vref_out_+_-13dBv
- R21 pad 1: GND -> GNDD
- R22 pad 1: Net-(J9-Pad3) -> vref_out_+_-10dBv
- R23 pad 1: GND -> GND2
- R23 pad 2: Net-(J9-Pad3) -> vref_out_+_-10dBv
- R24 pad 2: +9VA -> GND2
- R25 pad 1: GND -> -9VA
- R39 pad 1: Net-(J10-Pad1) -> Net-(C33-Pad1)
- R39 pad 2: GND -> +9VA
- R40 pad 1: -9VA -> Net-(C24-Pad1)
- R40 pad 2: Net-(J10-Pad1) -> +9VA
- R41 pad 1: Net-(J10-Pad3) -> -9VA
- R41 pad 2: GND -> vref_out_-_-10dBv
- R42 pad 1: -9VA -> vref_out_-_-10dBv
- R42 pad 2: Net-(J10-Pad3) -> GND2
- SW1 pad 1: Net-(J3-Pad1) -> Net-(J4-Pad1)
- U4 pad 1: GND -> GNDD
- U4 pad 6: Net-(C13-Pad1) -> Net-(C15-Pad1)
- U5 pad 1: GND -> GNDD
- U5 pad 7: Net-(C14-Pad2) -> Net-(C16-Pad2)
- U6 pad 1: Net-(C13-Pad1) -> Net-(C15-Pad1)
- U7 pad 2: Net-(C14-Pad2) -> Net-(C16-Pad2)
- U9 pad 10: vref_out_- -> vref_out_-_-10dBv
- U9 pad 12: -9VA -> Net-(C34-Pad1)
- U9 pad 13: Net-(D12-Pad1) -> Net-(D3-Pad1)
- U9 pad 14: Net-(D12-Pad1) -> Net-(D3-Pad1)
- U9 pad 3: +9VA -> Net-(C33-Pad1)
- U9 pad 4: vref_out_- -> vref_out_-_-10dBv
- U9 pad 7: vref_out_+ -> vref_out_+_-10dBv
- U9 pad 9: vref_out_+ -> vref_out_+_-10dBv
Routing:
- net +9VA: track 16.4 -> 240.8 mm, vias 0 -> 10
- net -9VA: track 15.4 -> 236.1 mm, vias 0 -> 11
- net mix_out_L: track 0.00 -> 169.1 mm, vias 0 -> 5
- net mix_out_R: track 0.00 -> 152.6 mm, vias 0 -> 7
- net BT_Mic_Out_P: track 0.00 -> 151.7 mm, vias 0 -> 2
- net in1_R: track 0.00 -> 79.6 mm
- net BT_in_R: track 0.00 -> 74.1 mm, vias 0 -> 1
- net BT_in_L: track 0.00 -> 73.7 mm, vias 0 -> 1
- net Net-(RV3-Pad3): track 0.00 -> 65.8 mm, vias 0 -> 2
- net Net-(RV3-Pad6): track 0.00 -> 60.2 mm, vias 0 -> 2
- net in1_L: track 0.00 -> 56.2 mm
- net Net-(J7-PadT): track 2.30 -> 58.0 mm, vias 0 -> 1
- net Net-(J3-Pad1): track 55.1 -> 0.00 mm
- net in2_R: track 0.00 -> 52.9 mm
- net Net-(J7-PadR): track 5.50 -> 57.3 mm, vias 0 -> 1
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- added copper zone on B.Cu, net GND2
- added copper zone on F.Cu, net GND2
- added copper zone on B.Cu, net GNDD
- added copper zone on F.Cu, net GNDD
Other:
- board size 150 x 59 mm -> 135 x 59 mm
- net class Default: via_dia 0.8 -> 1; via_drill 0.4 -> 0.6
- rule trace_min: 0.2 -> 0.254
- board text added: "-10dBv (Peak)"
- board text added: "-13dBv"
- board text added: "-Isolate |Common"
- board text added: "2020/11/24 Rev.A poyo"
- board text added: "BT Send Mix/Mic"
- board text added: "Bluetooth / Line 2"
- board text added: "GND Rx Tx"
- board text added: "L"
- board text added: "Line 1"
- board text added: "Line Mix Level"
- board text added: "Mic Gain 40dB/20dB"
- board text added: "Mic Mute UnMute/Mute"
- board text added: "Mic in (ECM)"
- board text added: "Monitor Out"
- board text added: "R"
- board text removed: "2020/8/24 poyo"
- board text removed: "40dB/20dB"
- board text removed: "DC5V only"
- board text removed: "Line in 2 / BT"
- board text removed: "Peak"

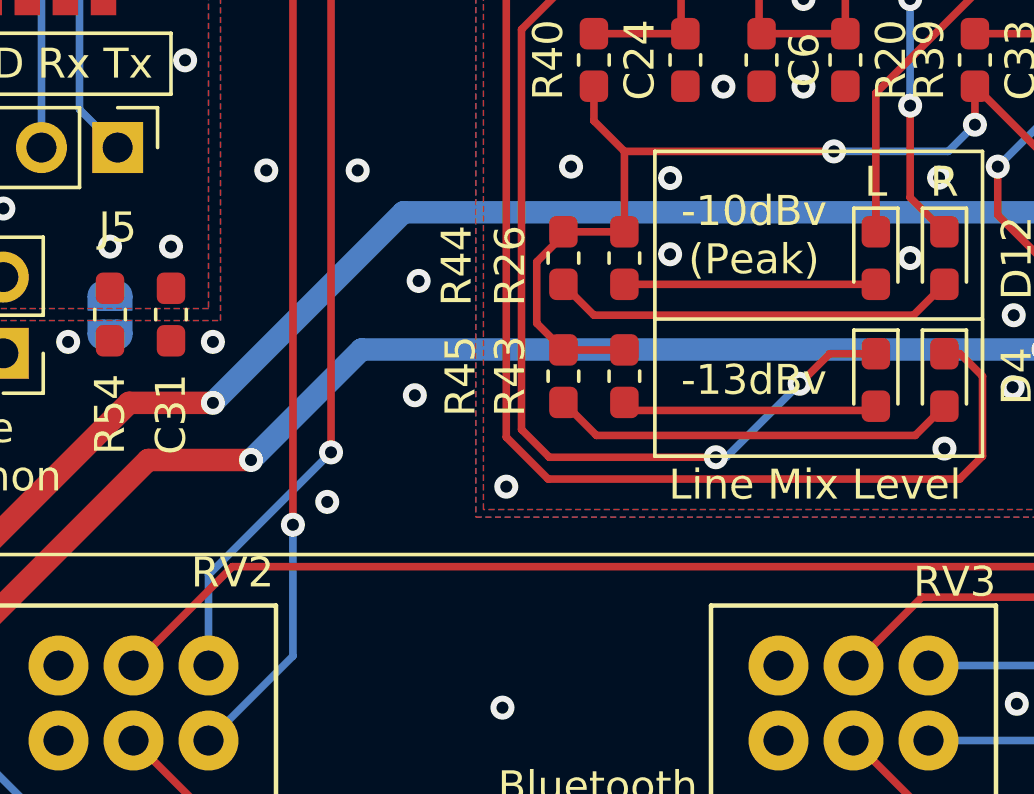
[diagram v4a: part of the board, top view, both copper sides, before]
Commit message: Fix Gerber Bug
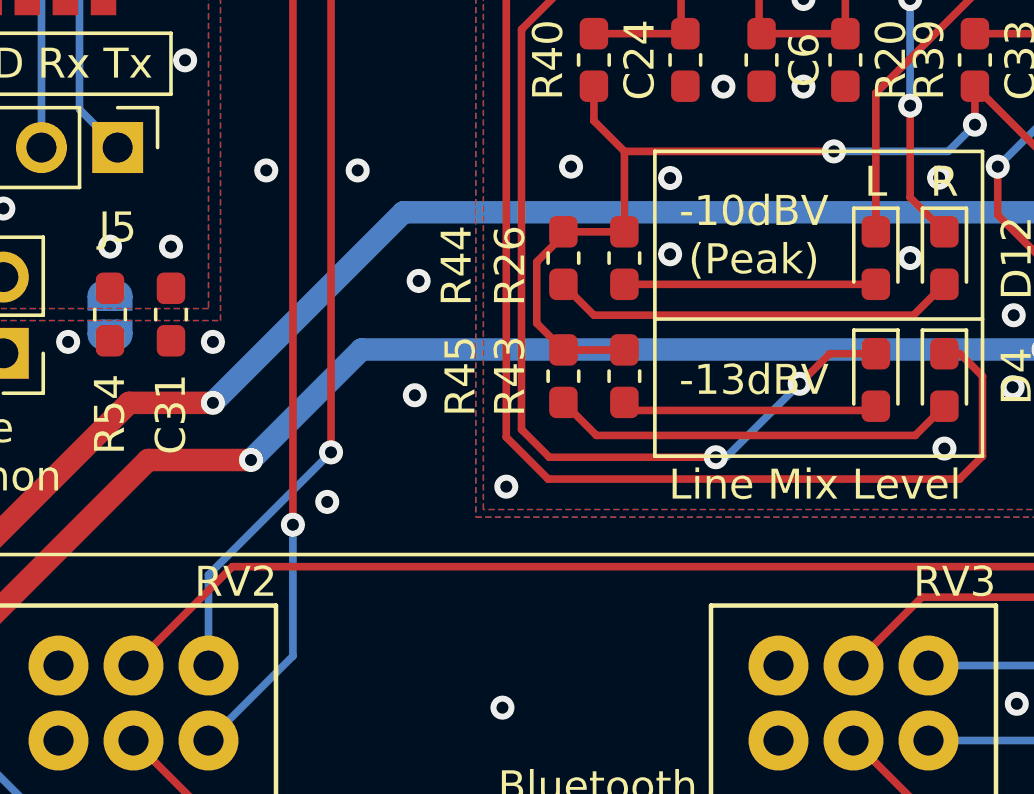
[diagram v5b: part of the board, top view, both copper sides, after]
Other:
- board text added: "-10dBV (Peak)"
- board text added: "-13dBV"
- board text removed: "-10dBv (Peak)"
- board text removed: "-13dBv"
